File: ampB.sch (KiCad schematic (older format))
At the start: 8 parts, among them U2 Mux, U3 MCP6004

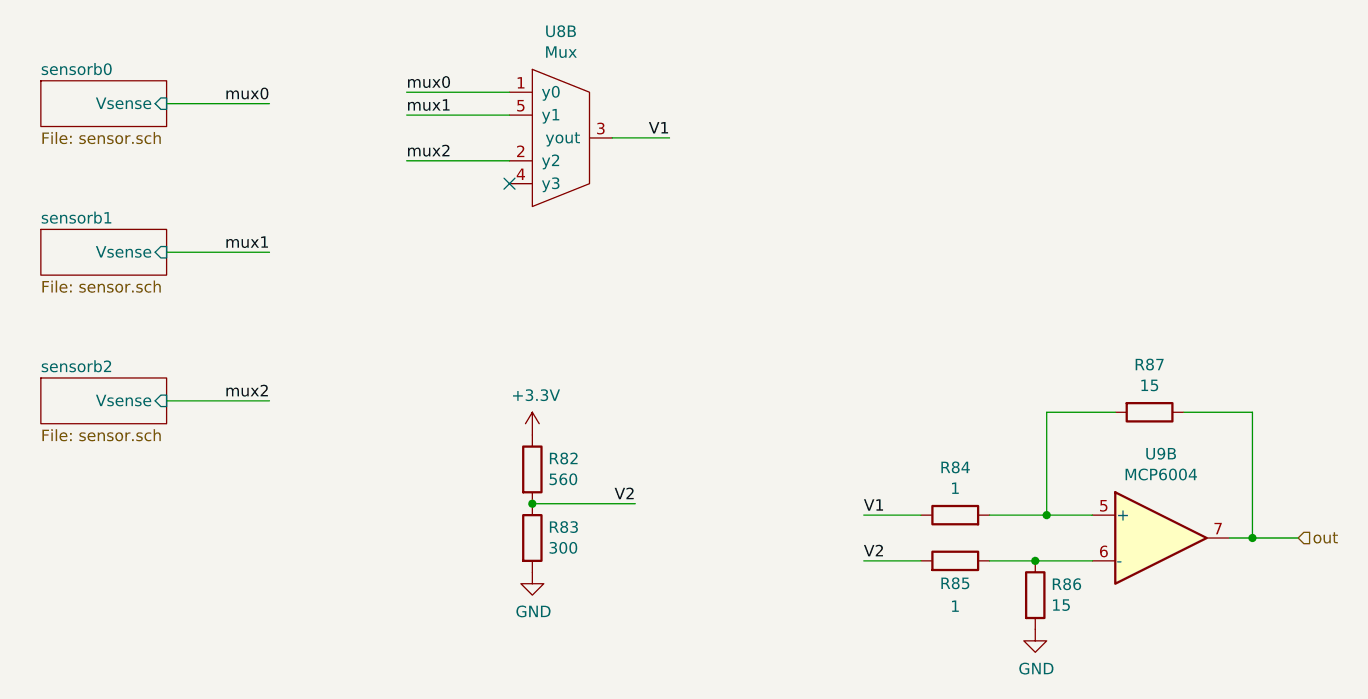
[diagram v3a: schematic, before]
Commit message: moved sensor r div to other side of mux
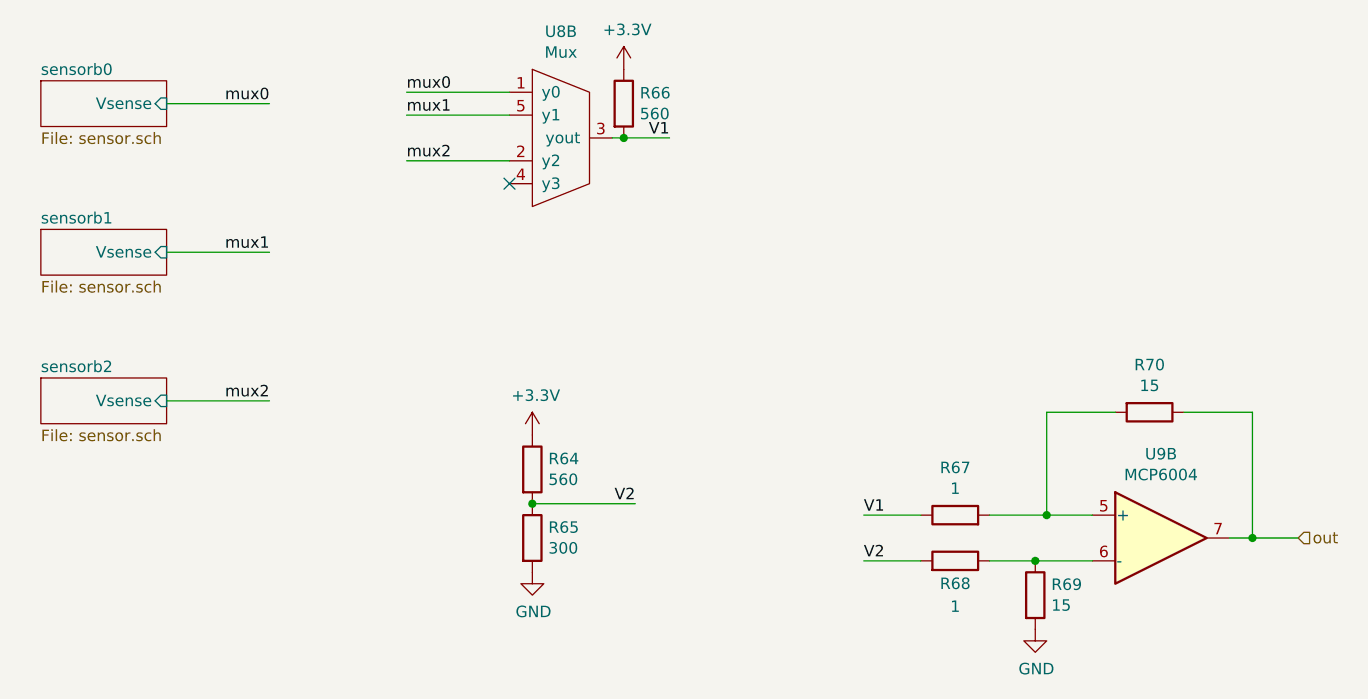
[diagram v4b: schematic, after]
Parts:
- added R10: 560, Resistor_THT:R_Axial_DIN0204_L3.6mm_D1.6mm_P5.08mm_Horizontal, symbol Device:R
- renumbered R12 to R11, R13 to R12, R14 to R13, R15 to R14, R10 to R8, R11 to R9
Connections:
- net +3V3: now also R10.1
- net V1: now also R10.2
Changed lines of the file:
@@
 $Descr A4 11693 8268
 encoding utf-8
-Sheet 38 41
+Sheet 6 41
 Title ""
 Date ""
@@
 AR Path="/6017CC5E/6019E3A5" Ref="R?"  Part="1"
 AR Path="/6017DA21/6019E3A5" Ref="R?"  Part="1"
-AR Path="/601927EB/6019E3A5" Ref="R14"  Part="1"
+AR Path="/601927EB/6019E3A5" Ref="R13"  Part="1"
 AR Path="/6019DBCE/6019E3A5" Ref="R?"  Part="1"
-AR Path="/601B4C11/6019E3A5" Ref="R50"  Part="1"
-AR Path="/601B73BA/6019E3A5" Ref="R86"  Part="1"
-F 0 "R86" H 5520 4096 50  0000 L CNN
+AR Path="/601B4C11/6019E3A5" Ref="R41"  Part="1"
+AR Path="/601B73BA/6019E3A5" Ref="R69"  Part="1"
+F 0 "R69" H 5520 4096 50  0000 L CNN
 F 1 "15" H 5520 4005 50  0000 L CNN
 F 2 "Resistor_THT:R_Axial_DIN0204_L3.6mm_D1.6mm_P5.08mm_Horizontal" V 5380 4050 50  0001 C CNN
@@
 AR Path="/6017CC5E/6017E430" Ref="R?"  Part="1"
 AR Path="/6017DA21/6017E430" Ref="R?"  Part="1"
-AR Path="/601927EB/6017E430" Ref="R15"  Part="1"
+AR Path="/601927EB/6017E430" Ref="R14"  Part="1"
 AR Path="/6019DBCE/6017E430" Ref="R?"  Part="1"
-AR Path="/601B4C11/6017E430" Ref="R51"  Part="1"
-AR Path="/601B73BA/6017E430" Ref="R87"  Part="1"
-F 0 "R87" V 5743 3250 50  0000 C CNN
+AR Path="/601B4C11/6017E430" Ref="R42"  Part="1"
+AR Path="/601B73BA/6017E430" Ref="R70"  Part="1"
+F 0 "R70" V 5743 3250 50  0000 C CNN
 F 1 "15" V 5834 3250 50  0000 C CNN
 F 2 "Resistor_THT:R_Axial_DIN0204_L3.6mm_D1.6mm_P5.08mm_Horizontal" V 5880 3250 50  0001 C CNN
@@
 AR Path="/6017CC5E/60198F33" Ref="R?"  Part="1"
 AR Path="/6017DA21/60198F33" Ref="R?"  Part="1"
-AR Path="/601927EB/60198F33" Ref="R12"  Part="1"
+AR Path="/601927EB/60198F33" Ref="R11"  Part="1"
 AR Path="/6019DBCE/60198F33" Ref="R?"  Part="1"
-AR Path="/601B4C11/60198F33" Ref="R48"  Part="1"
-AR Path="/601B73BA/60198F33" Ref="R84"  Part="1"
-F 0 "R84" V 5307 3700 50  0000 C CNN
+AR Path="/601B4C11/60198F33" Ref="R39"  Part="1"
+AR Path="/601B73BA/60198F33" Ref="R67"  Part="1"
+F 0 "R67" V 5307 3700 50  0000 C CNN
 F 1 "1" V 5216 3700 50  0000 C CNN
 F 2 "Resistor_THT:R_Axial_DIN0204_L3.6mm_D1.6mm_P5.08mm_Horizontal" V 5030 3700 50  0001 C CNN
@@
 AR Path="/6017CC5E/6017E432" Ref="R?"  Part="1"
 AR Path="/6017DA21/6017E432" Ref="R?"  Part="1"
-AR Path="/601927EB/6017E432" Ref="R13"  Part="1"
+AR Path="/601927EB/6017E432" Ref="R12"  Part="1"
 AR Path="/6019DBCE/6017E432" Ref="R?"  Part="1"
-AR Path="/601B4C11/6017E432" Ref="R49"  Part="1"
-AR Path="/601B73BA/6017E432" Ref="R85"  Part="1"
-F 0 "R85" V 5000 3900 50  0000 C CNN
+AR Path="/601B4C11/6017E432" Ref="R40"  Part="1"
+AR Path="/601B73BA/6017E432" Ref="R68"  Part="1"
+F 0 "R68" V 5000 3900 50  0000 C CNN
 F 1 "1" V 4900 3900 50  0000 C CNN
 F 2 "Resistor_THT:R_Axial_DIN0204_L3.6mm_D1.6mm_P5.08mm_Horizontal" V 5030 3900 50  0001 C CNN
@@
 	4950 3900 4700 3900
 Wire Wire Line
-	3600 2050 3850 2050
+	3600 2050 3650 2050
 Text Label 3850 2050 2    50   ~ 0
 V1
@@
 AR Path="/6017CC5E/60198F35" Ref="R?"  Part="1"
 AR Path="/6017DA21/60198F35" Ref="R?"  Part="1"
-AR Path="/601927EB/60198F35" Ref="R10"  Part="1"
+AR Path="/601927EB/60198F35" Ref="R8"  Part="1"
 AR Path="/6019DBCE/60198F35" Ref="R?"  Part="1"
-AR Path="/601B4C11/60198F35" Ref="R46"  Part="1"
-AR Path="/601B73BA/60198F35" Ref="R82"  Part="1"
-F 0 "R82" H 3320 3546 50  0000 L CNN
+AR Path="/601B4C11/60198F35" Ref="R36"  Part="1"
+AR Path="/601B73BA/60198F35" Ref="R64"  Part="1"
+F 0 "R64" H 3320 3546 50  0000 L CNN
 F 1 "560" H 3320 3455 50  0000 L CNN
 F 2 "Resistor_THT:R_Axial_DIN0204_L3.6mm_D1.6mm_P5.08mm_Horizontal" V 3180 3500 50  0001 C CNN
@@
 AR Path="/6017CC5E/6019E3B4" Ref="R?"  Part="1"
 AR Path="/6017DA21/6019E3B4" Ref="R?"  Part="1"
-AR Path="/601927EB/6019E3B4" Ref="R11"  Part="1"
+AR Path="/601927EB/6019E3B4" Ref="R9"  Part="1"
 AR Path="/6019DBCE/6019E3B4" Ref="R?"  Part="1"
-AR Path="/601B4C11/6019E3B4" Ref="R47"  Part="1"
-AR Path="/601B73BA/6019E3B4" Ref="R83"  Part="1"
-F 0 "R83" H 3320 3846 50  0000 L CNN
+AR Path="/601B4C11/6019E3B4" Ref="R37"  Part="1"
+AR Path="/601B73BA/6019E3B4" Ref="R65"  Part="1"
+F 0 "R65" H 3320 3846 50  0000 L CNN
 F 1 "300" H 3320 3755 50  0000 L CNN
 F 2 "Resistor_THT:R_Axial_DIN0204_L3.6mm_D1.6mm_P5.08mm_Horizontal" V 3180 3800 50  0001 C CNN
@@
 AR Path="/6017CC5E/6019E3B5" Ref="#PWR?"  Part="1"
 AR Path="/6017DA21/6019E3B5" Ref="#PWR?"  Part="1"
-AR Path="/601927EB/6019E3B5" Ref="#PWR021"  Part="1"
+AR Path="/601927EB/6019E3B5" Ref="#PWR019"  Part="1"
 AR Path="/6019DBCE/6019E3B5" Ref="#PWR?"  Part="1"
-AR Path="/601B4C11/6019E3B5" Ref="#PWR063"  Part="1"
-AR Path="/601B73BA/6019E3B5" Ref="#PWR0105"  Part="1"
-F 0 "#PWR0105" H 3250 3200 50  0001 C CNN
+AR Path="/601B4C11/6019E3B5" Ref="#PWR053"  Part="1"
+AR Path="/601B73BA/6019E3B5" Ref="#PWR087"  Part="1"
+F 0 "#PWR087" H 3250 3200 50  0001 C CNN
 F 1 "+3.3V" H 3265 3523 50  0000 C CNN
 F 2 "" H 3250 3350 50  0001 C CNN
@@
 AR Path="/6017CC5E/6017E436" Ref="#PWR?"  Part="1"
 AR Path="/6017DA21/6017E436" Ref="#PWR?"  Part="1"
-AR Path="/601927EB/6017E436" Ref="#PWR022"  Part="1"
+AR Path="/601927EB/6017E436" Ref="#PWR020"  Part="1"
 AR Path="/6019DBCE/6017E436" Ref="#PWR?"  Part="1"
-AR Path="/601B4C11/6017E436" Ref="#PWR064"  Part="1"
-AR Path="/601B73BA/6017E436" Ref="#PWR0106"  Part="1"
-F 0 "#PWR0106" H 3250 3700 50  0001 C CNN
+AR Path="/601B4C11/6017E436" Ref="#PWR054"  Part="1"
+AR Path="/601B73BA/6017E436" Ref="#PWR088"  Part="1"
+F 0 "#PWR088" H 3250 3700 50  0001 C CNN
 F 1 "GND" H 3255 3777 50  0000 C CNN
 F 2 "" H 3250 3950 50  0001 C CNN
@@
 AR Path="/6017CC5E/6019E3AC" Ref="#PWR?"  Part="1"
 AR Path="/6017DA21/6019E3AC" Ref="#PWR?"  Part="1"
-AR Path="/601927EB/6019E3AC" Ref="#PWR023"  Part="1"
+AR Path="/601927EB/6019E3AC" Ref="#PWR022"  Part="1"
 AR Path="/6019DBCE/6019E3AC" Ref="#PWR?"  Part="1"
-AR Path="/601B4C11/6019E3AC" Ref="#PWR065"  Part="1"
-AR Path="/601B73BA/6019E3AC" Ref="#PWR0107"  Part="1"
-F 0 "#PWR0107" H 5450 3950 50  0001 C CNN
+AR Path="/601B4C11/6019E3AC" Ref="#PWR056"  Part="1"
+AR Path="/601B73BA/6019E3AC" Ref="#PWR090"  Part="1"
+F 0 "#PWR090" H 5450 3950 50  0001 C CNN
 F 1 "GND" H 5455 4027 50  0000 C CNN
 F 2 "" H 5450 4200 50  0001 C CNN
@@
 F2 "Vsense" I R 1650 3200 50
 $EndSheet
+$Comp
+L Device:R R?
+U 1 1 602069C8
+P 3650 1900
+AR Path="/60132BC3/6013AE22/602069C8" Ref="R?"  Part="1"
+AR Path="/6017CC5E/602069C8" Ref="R?"  Part="1"
+AR Path="/6017DA21/602069C8" Ref="R?"  Part="1"
+AR Path="/601927EB/602069C8" Ref="R10"  Part="1"
+AR Path="/6019DBCE/602069C8" Ref="R?"  Part="1"
+AR Path="/601B4C11/602069C8" Ref="R38"  Part="1"
+AR Path="/601B73BA/602069C8" Ref="R66"  Part="1"
+F 0 "R66" H 3720 1946 50  0000 L CNN
+F 1 "560" H 3720 1855 50  0000 L CNN
+F 2 "Resistor_THT:R_Axial_DIN0204_L3.6mm_D1.6mm_P5.08mm_Horizontal" V 3580 1900 50  0001 C CNN
+F 3 "~" H 3650 1900 50  0001 C CNN
+	1    3650 1900
+	1    0    0    -1
+$EndComp
+Connection ~ 3650 2050
+Wire Wire Line
+	3650 2050 3850 2050
+$Comp
+L power:+3.3V #PWR?
+U 1 1 60206B01
+P 3650 1750
+AR Path="/60132BC3/6013AE22/60206B01" Ref="#PWR?"  Part="1"
+AR Path="/6017CC5E/60206B01" Ref="#PWR?"  Part="1"
+AR Path="/6017DA21/60206B01" Ref="#PWR?"  Part="1"
+AR Path="/601927EB/60206B01" Ref="#PWR021"  Part="1"
+AR Path="/6019DBCE/60206B01" Ref="#PWR?"  Part="1"
+AR Path="/601B4C11/60206B01" Ref="#PWR055"  Part="1"
+AR Path="/601B73BA/60206B01" Ref="#PWR089"  Part="1"
+F 0 "#PWR089" H 3650 1600 50  0001 C CNN
+F 1 "+3.3V" H 3665 1923 50  0000 C CNN
+F 2 "" H 3650 1750 50  0001 C CNN
+F 3 "" H 3650 1750 50  0001 C CNN
+	1    3650 1750
+	1    0    0    -1
+$EndComp
 $EndSCHEMATC

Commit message: fixed drc errors
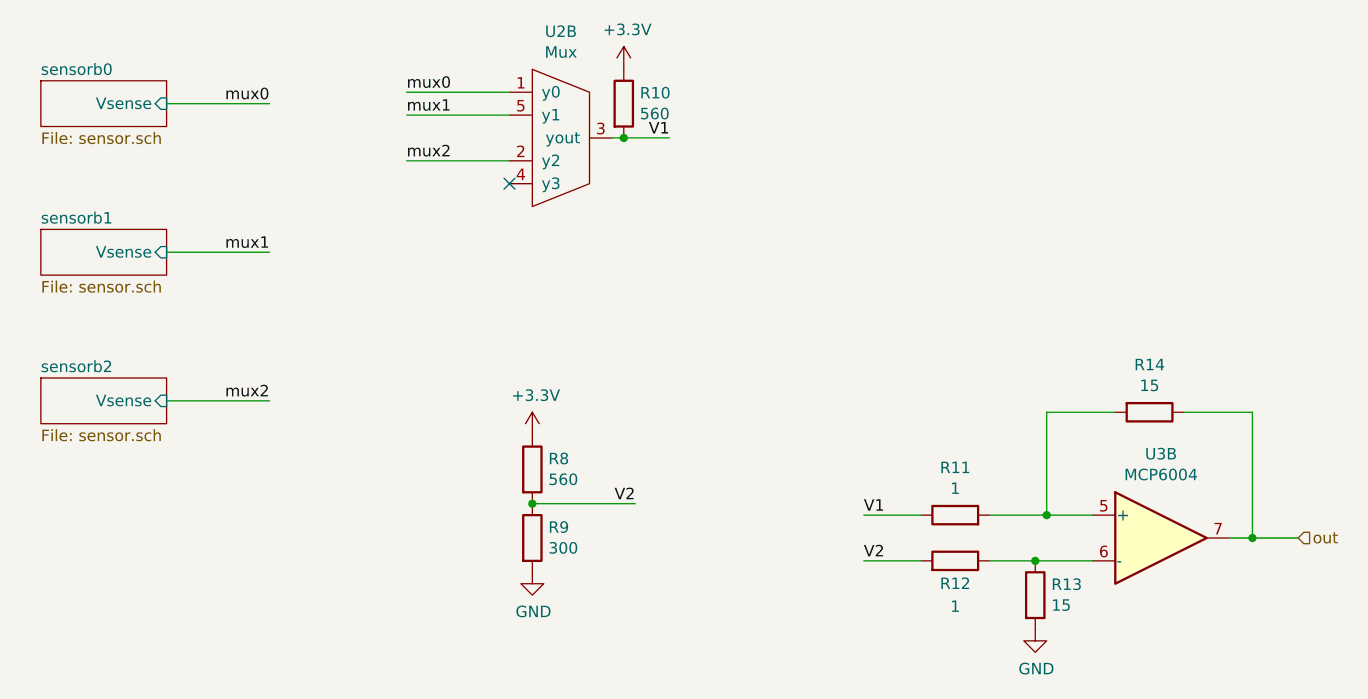
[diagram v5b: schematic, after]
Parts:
- U2: footprint Package_DIP:DIP-16_W7.62mm -> Package_SO:SOIC-16_3.9x9.9mm_P1.27mm
- U3: footprint Package_DIP:DIP-14_W7.62mm -> Package_SO:SOIC-16_3.9x9.9mm_P1.27mm
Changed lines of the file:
@@
 AR Path="/601B4C11/6019E3A5" Ref="R41"  Part="1"
 AR Path="/601B73BA/6019E3A5" Ref="R69"  Part="1"
-F 0 "R69" H 5520 4096 50  0000 L CNN
+F 0 "R13" H 5520 4096 50  0000 L CNN
 F 1 "15" H 5520 4005 50  0000 L CNN
 F 2 "Resistor_THT:R_Axial_DIN0204_L3.6mm_D1.6mm_P5.08mm_Horizontal" V 5380 4050 50  0001 C CNN
@@
 AR Path="/601B4C11/6017E430" Ref="R42"  Part="1"
 AR Path="/601B73BA/6017E430" Ref="R70"  Part="1"
-F 0 "R70" V 5743 3250 50  0000 C CNN
+F 0 "R14" V 5743 3250 50  0000 C CNN
 F 1 "15" V 5834 3250 50  0000 C CNN
 F 2 "Resistor_THT:R_Axial_DIN0204_L3.6mm_D1.6mm_P5.08mm_Horizontal" V 5880 3250 50  0001 C CNN
@@
 AR Path="/601B4C11/60198F33" Ref="R39"  Part="1"
 AR Path="/601B73BA/60198F33" Ref="R67"  Part="1"
-F 0 "R67" V 5307 3700 50  0000 C CNN
+F 0 "R11" V 5307 3700 50  0000 C CNN
 F 1 "1" V 5216 3700 50  0000 C CNN
 F 2 "Resistor_THT:R_Axial_DIN0204_L3.6mm_D1.6mm_P5.08mm_Horizontal" V 5030 3700 50  0001 C CNN
@@
 AR Path="/601B4C11/6017E432" Ref="R40"  Part="1"
 AR Path="/601B73BA/6017E432" Ref="R68"  Part="1"
-F 0 "R68" V 5000 3900 50  0000 C CNN
+F 0 "R12" V 5000 3900 50  0000 C CNN
 F 1 "1" V 4900 3900 50  0000 C CNN
 F 2 "Resistor_THT:R_Axial_DIN0204_L3.6mm_D1.6mm_P5.08mm_Horizontal" V 5030 3900 50  0001 C CNN
@@
 AR Path="/601B4C11/60198F35" Ref="R36"  Part="1"
 AR Path="/601B73BA/60198F35" Ref="R64"  Part="1"
-F 0 "R64" H 3320 3546 50  0000 L CNN
+F 0 "R8" H 3320 3546 50  0000 L CNN
 F 1 "560" H 3320 3455 50  0000 L CNN
 F 2 "Resistor_THT:R_Axial_DIN0204_L3.6mm_D1.6mm_P5.08mm_Horizontal" V 3180 3500 50  0001 C CNN
@@
 AR Path="/601B4C11/6019E3B4" Ref="R37"  Part="1"
 AR Path="/601B73BA/6019E3B4" Ref="R65"  Part="1"
-F 0 "R65" H 3320 3846 50  0000 L CNN
+F 0 "R9" H 3320 3846 50  0000 L CNN
 F 1 "300" H 3320 3755 50  0000 L CNN
 F 2 "Resistor_THT:R_Axial_DIN0204_L3.6mm_D1.6mm_P5.08mm_Horizontal" V 3180 3800 50  0001 C CNN
@@
 AR Path="/601B4C11/6017859B" Ref="U5"  Part="2"
 AR Path="/601B73BA/6017859B" Ref="U8"  Part="2"
-F 0 "U8" H 3375 2515 50  0000 C CNN
+F 0 "U2" H 3375 2515 50  0000 C CNN
 F 1 "Mux" H 3375 2424 50  0000 C CNN
-F 2 "Package_DIP:DIP-16_W7.62mm" H 3350 2050 50  0001 C CNN
+F 2 "Package_SO:SOIC-16_3.9x9.9mm_P1.27mm" H 3350 2050 50  0001 C CNN
 F 3 "" H 3350 2050 50  0001 C CNN
 	2    3350 2050
@@
 AR Path="/601B4C11/6018C8DB" Ref="U6"  Part="2"
 AR Path="/601B73BA/6018C8DB" Ref="U9"  Part="2"
-F 0 "U9" H 6000 4167 50  0000 C CNN
+F 0 "U3" H 6000 4167 50  0000 C CNN
 F 1 "MCP6004" H 6000 4076 50  0000 C CNN
-F 2 "Package_DIP:DIP-14_W7.62mm" H 5950 3900 50  0001 C CNN
+F 2 "Package_SO:SOIC-16_3.9x9.9mm_P1.27mm" H 5950 3900 50  0001 C CNN
 F 3 "http://ww1.microchip.com/downloads/en/DeviceDoc/21733j.pdf" H 6050 4000 50  0001 C CNN
 	2    6000 3800
@@
 AR Path="/601B4C11/602069C8" Ref="R38"  Part="1"
 AR Path="/601B73BA/602069C8" Ref="R66"  Part="1"
-F 0 "R66" H 3720 1946 50  0000 L CNN
+F 0 "R10" H 3720 1946 50  0000 L CNN
 F 1 "560" H 3720 1855 50  0000 L CNN
 F 2 "Resistor_THT:R_Axial_DIN0204_L3.6mm_D1.6mm_P5.08mm_Horizontal" V 3580 1900 50  0001 C CNN

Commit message: changed solder pads to be two separate footprints
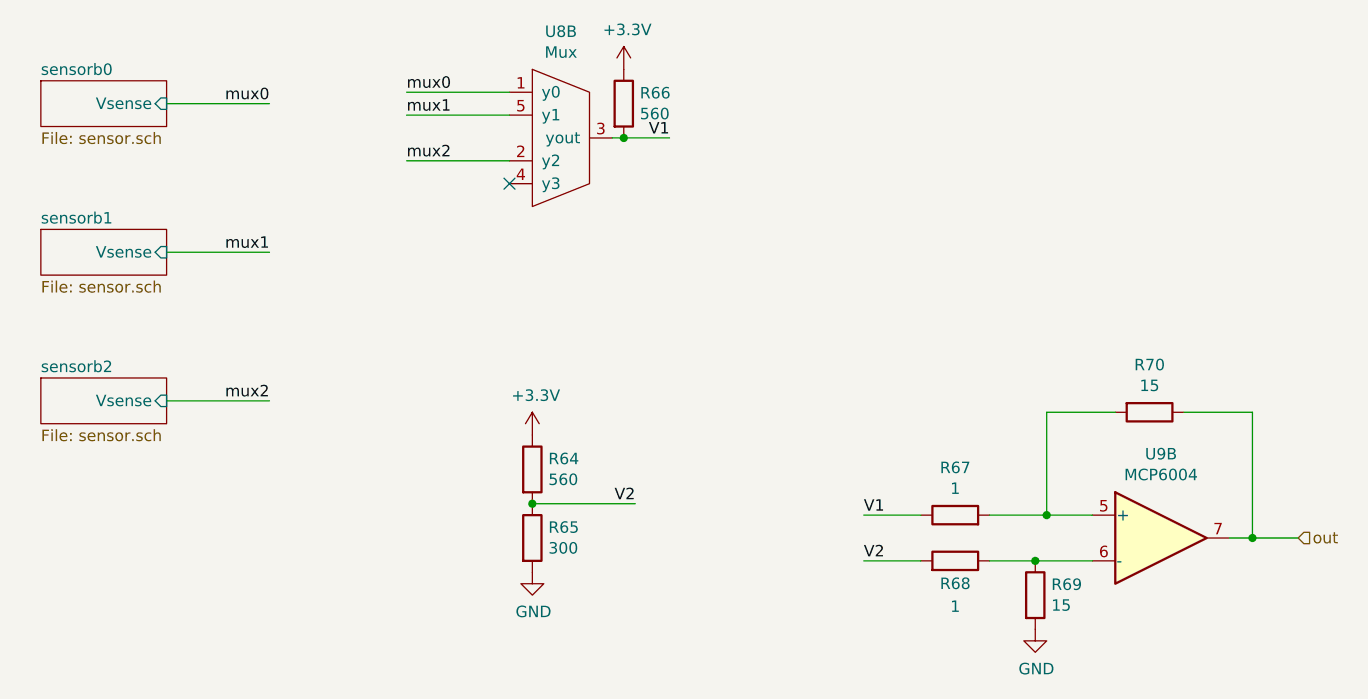
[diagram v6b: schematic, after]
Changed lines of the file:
@@
 AR Path="/601B4C11/6019E3A5" Ref="R41"  Part="1"
 AR Path="/601B73BA/6019E3A5" Ref="R69"  Part="1"
-F 0 "R13" H 5520 4096 50  0000 L CNN
+F 0 "R69" H 5520 4096 50  0000 L CNN
 F 1 "15" H 5520 4005 50  0000 L CNN
 F 2 "Resistor_THT:R_Axial_DIN0204_L3.6mm_D1.6mm_P5.08mm_Horizontal" V 5380 4050 50  0001 C CNN
@@
 AR Path="/601B4C11/6017E430" Ref="R42"  Part="1"
 AR Path="/601B73BA/6017E430" Ref="R70"  Part="1"
-F 0 "R14" V 5743 3250 50  0000 C CNN
+F 0 "R70" V 5743 3250 50  0000 C CNN
 F 1 "15" V 5834 3250 50  0000 C CNN
 F 2 "Resistor_THT:R_Axial_DIN0204_L3.6mm_D1.6mm_P5.08mm_Horizontal" V 5880 3250 50  0001 C CNN
@@
 AR Path="/601B4C11/60198F33" Ref="R39"  Part="1"
 AR Path="/601B73BA/60198F33" Ref="R67"  Part="1"
-F 0 "R11" V 5307 3700 50  0000 C CNN
+F 0 "R67" V 5307 3700 50  0000 C CNN
 F 1 "1" V 5216 3700 50  0000 C CNN
 F 2 "Resistor_THT:R_Axial_DIN0204_L3.6mm_D1.6mm_P5.08mm_Horizontal" V 5030 3700 50  0001 C CNN
@@
 AR Path="/601B4C11/6017E432" Ref="R40"  Part="1"
 AR Path="/601B73BA/6017E432" Ref="R68"  Part="1"
-F 0 "R12" V 5000 3900 50  0000 C CNN
+F 0 "R68" V 5000 3900 50  0000 C CNN
 F 1 "1" V 4900 3900 50  0000 C CNN
 F 2 "Resistor_THT:R_Axial_DIN0204_L3.6mm_D1.6mm_P5.08mm_Horizontal" V 5030 3900 50  0001 C CNN
@@
 AR Path="/601B4C11/60198F35" Ref="R36"  Part="1"
 AR Path="/601B73BA/60198F35" Ref="R64"  Part="1"
-F 0 "R8" H 3320 3546 50  0000 L CNN
+F 0 "R64" H 3320 3546 50  0000 L CNN
 F 1 "560" H 3320 3455 50  0000 L CNN
 F 2 "Resistor_THT:R_Axial_DIN0204_L3.6mm_D1.6mm_P5.08mm_Horizontal" V 3180 3500 50  0001 C CNN
@@
 AR Path="/601B4C11/6019E3B4" Ref="R37"  Part="1"
 AR Path="/601B73BA/6019E3B4" Ref="R65"  Part="1"
-F 0 "R9" H 3320 3846 50  0000 L CNN
+F 0 "R65" H 3320 3846 50  0000 L CNN
 F 1 "300" H 3320 3755 50  0000 L CNN
 F 2 "Resistor_THT:R_Axial_DIN0204_L3.6mm_D1.6mm_P5.08mm_Horizontal" V 3180 3800 50  0001 C CNN
@@
 AR Path="/601B4C11/6017859B" Ref="U5"  Part="2"
 AR Path="/601B73BA/6017859B" Ref="U8"  Part="2"
-F 0 "U2" H 3375 2515 50  0000 C CNN
+F 0 "U8" H 3375 2515 50  0000 C CNN
 F 1 "Mux" H 3375 2424 50  0000 C CNN
 F 2 "Package_SO:SOIC-16_3.9x9.9mm_P1.27mm" H 3350 2050 50  0001 C CNN
@@
 AR Path="/601B4C11/6018C8DB" Ref="U6"  Part="2"
 AR Path="/601B73BA/6018C8DB" Ref="U9"  Part="2"
-F 0 "U3" H 6000 4167 50  0000 C CNN
+F 0 "U9" H 6000 4167 50  0000 C CNN
 F 1 "MCP6004" H 6000 4076 50  0000 C CNN
 F 2 "Package_SO:SOIC-16_3.9x9.9mm_P1.27mm" H 5950 3900 50  0001 C CNN
@@
 AR Path="/601B4C11/602069C8" Ref="R38"  Part="1"
 AR Path="/601B73BA/602069C8" Ref="R66"  Part="1"
-F 0 "R10" H 3720 1946 50  0000 L CNN
+F 0 "R66" H 3720 1946 50  0000 L CNN
 F 1 "560" H 3720 1855 50  0000 L CNN
 F 2 "Resistor_THT:R_Axial_DIN0204_L3.6mm_D1.6mm_P5.08mm_Horizontal" V 3580 1900 50  0001 C CNN
